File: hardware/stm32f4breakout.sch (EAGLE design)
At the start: 18 parts, among them U101 STM32F427VGT6, X101 24MHz

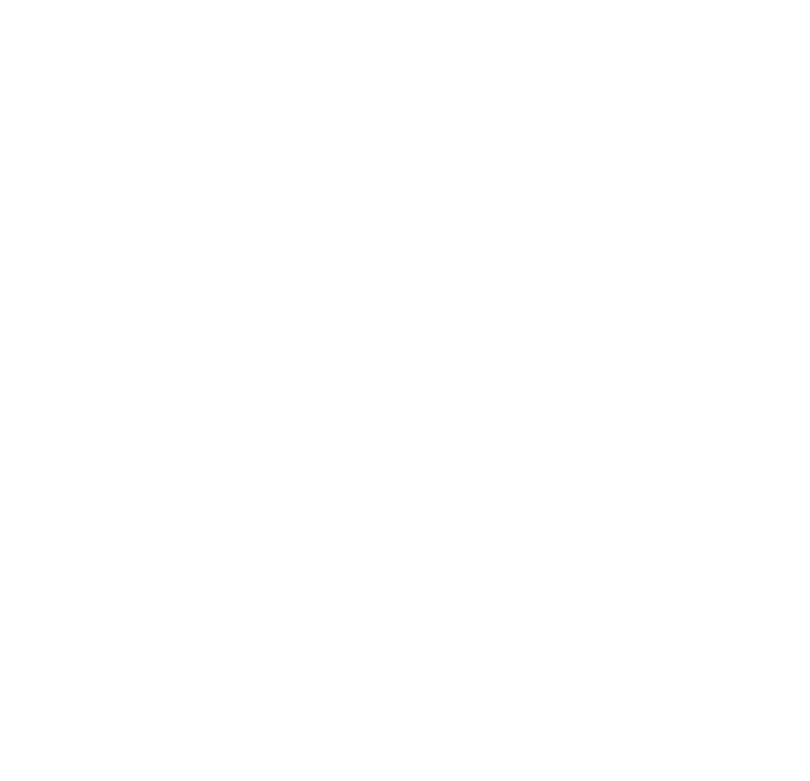
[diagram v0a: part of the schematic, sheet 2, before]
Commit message: Add 4.7uF decoupling cap
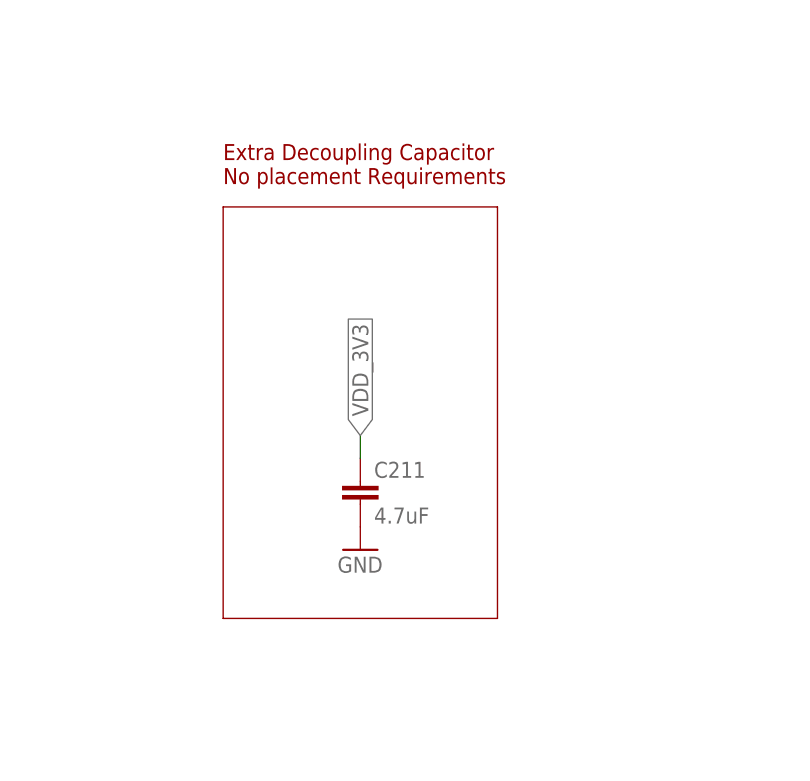
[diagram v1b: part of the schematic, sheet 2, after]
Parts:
- added C211: 4.7uF, quad:C-EUC0603
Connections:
- net GND: now also C211.2
- net VDD_3V3: now also C211.1
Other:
- note added: "Extra Decoupling Capacitor No placement Requirements"
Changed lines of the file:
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@@
 <grid distance="0.1" unitdist="inch" unit="inch" style="lines" multiple="1" display="no" altdistance="0.01" altunitdist="inch" altunit="inch"/>
 <layers>
-<layer number="1" name="Top" color="4" fill="1" visible="no" active="no"/>
-<layer number="2" name="Route2" color="1" fill="3" visible="no" active="no"/>
-<layer number="3" name="Route3" color="4" fill="3" visible="no" active="no"/>
-<layer number="4" name="Route4" color="1" fill="4" visible="no" active="no"/>
-<layer number="5" name="Route5" color="4" fill="4" visible="no" active="no"/>
-<layer number="6" name="Route6" color="1" fill="8" visible="no" active="no"/>
-<layer number="7" name="Route7" color="4" fill="8" visible="no" active="no"/>
-<layer number="8" name="Route8" color="1" fill="2" visible="no" active="no"/>
-<layer number="9" name="Route9" color="4" fill="2" visible="no" active="no"/>
-<layer number="10" name="Route10" color="1" fill="7" visible="no" active="no"/>
-<layer number="11" name="Route11" color="4" fill="7" visible="no" active="no"/>
-<layer number="12" name="Route12" color="1" fill="5" visible="no" active="no"/>
-<layer number="13" name="Route13" color="4" fill="5" visible="no" active="no"/>
-<layer number="14" name="Route14" color="1" fill="6" visible="no" active="no"/>
-<layer number="15" name="Route15" color="4" fill="6" visible="no" active="no"/>
-<layer number="16" name="Bottom" color="1" fill="1" visible="no" active="no"/>
-<layer number="17" name="Pads" color="2" fill="1" visible="no" active="no"/>
-<layer number="18" name="Vias" color="2" fill="1" visible="no" active="no"/>
-<layer number="19" name="Unrouted" color="6" fill="1" visible="no" active="no"/>
-<layer number="20" name="Dimension" color="24" fill="1" visible="no" active="no"/>
-<layer number="21" name="tPlace" color="7" fill="1" visible="no" active="no"/>
-<layer number="22" name="bPlace" color="7" fill="1" visible="no" active="no"/>
-<layer number="23" name="tOrigins" color="15" fill="1" visible="no" active="no"/>
-<layer number="24" name="bOrigins" color="15" fill="1" visible="no" active="no"/>
-<layer number="25" name="tNames" color="7" fill="1" visible="no" active="no"/>
-<layer number="26" name="bNames" color="7" fill="1" visible="no" active="no"/>
-<layer number="27" name="tValues" color="7" fill="1" visible="no" active="no"/>
-<layer number="28" name="bValues" color="7" fill="1" visible="no" active="no"/>
+<layer number="1" name="Top" color="4" fill="1" visible="yes" active="no"/>
+<layer number="2" name="Route2" color="1" fill="3" visible="yes" active="no"/>
+<layer number="3" name="Route3" color="4" fill="3" visible="yes" active="no"/>
+<layer number="4" name="Route4" color="1" fill="4" visible="yes" active="no"/>
+<layer number="5" name="Route5" color="4" fill="4" visible="yes" active="no"/>
+<layer number="6" name="Route6" color="1" fill="8" visible="yes" active="no"/>
+<layer number="7" name="Route7" color="4" fill="8" visible="yes" active="no"/>
+<layer number="8" name="Route8" color="1" fill="2" visible="yes" active="no"/>
+<layer number="9" name="Route9" color="4" fill="2" visible="yes" active="no"/>
+<layer number="10" name="Route10" color="1" fill="7" visible="yes" active="no"/>
+<layer number="11" name="Route11" color="4" fill="7" visible="yes" active="no"/>
+<layer number="12" name="Route12" color="1" fill="5" visible="yes" active="no"/>
+<layer number="13" name="Route13" color="4" fill="5" visible="yes" active="no"/>
+<layer number="14" name="Route14" color="1" fill="6" visible="yes" active="no"/>
+<layer number="15" name="Route15" color="4" fill="6" visible="yes" active="no"/>
+<layer number="16" name="Bottom" color="1" fill="1" visible="yes" active="no"/>
+<layer number="17" name="Pads" color="2" fill="1" visible="yes" active="no"/>
+<layer number="18" name="Vias" color="2" fill="1" visible="yes" active="no"/>
+<layer number="19" name="Unrouted" color="6" fill="1" visible="yes" active="no"/>
+<layer number="20" name="Dimension" color="24" fill="1" visible="yes" active="no"/>
+<layer number="21" name="tPlace" color="7" fill="1" visible="yes" active="no"/>
+<layer number="22" name="bPlace" color="7" fill="1" visible="yes" active="no"/>
+<layer number="23" name="tOrigins" color="15" fill="1" visible="yes" active="no"/>
+<layer number="24" name="bOrigins" color="15" fill="1" visible="yes" active="no"/>
+<layer number="25" name="tNames" color="7" fill="1" visible="yes" active="no"/>
+<layer number="26" name="bNames" color="7" fill="1" visible="yes" active="no"/>
+<layer number="27" name="tValues" color="7" fill="1" visible="yes" active="no"/>
+<layer number="28" name="bValues" color="7" fill="1" visible="yes" active="no"/>
 <layer number="29" name="tStop" color="7" fill="3" visible="no" active="no"/>
 <layer number="30" name="bStop" color="7" fill="6" visible="no" active="no"/>
@@
 <layer number="35" name="tGlue" color="7" fill="4" visible="no" active="no"/>
 <layer number="36" name="bGlue" color="7" fill="5" visible="no" active="no"/>
-<layer number="37" name="tTest" color="7" fill="1" visible="no" active="no"/>
-<layer number="38" name="bTest" color="7" fill="1" visible="no" active="no"/>
+<layer number="37" name="tTest" color="7" fill="1" visible="yes" active="no"/>
+<layer number="38" name="bTest" color="7" fill="1" visible="yes" active="no"/>
 <layer number="39" name="tKeepout" color="4" fill="11" visible="no" active="no"/>
 <layer number="40" name="bKeepout" color="1" fill="11" visible="no" active="no"/>
@@
 <layer number="44" name="Drills" color="7" fill="1" visible="no" active="no"/>
 <layer number="45" name="Holes" color="7" fill="1" visible="no" active="no"/>
-<layer number="46" name="Milling" color="3" fill="1" visible="no" active="no"/>
-<layer number="47" name="Measures" color="7" fill="1" visible="no" active="no"/>
-<layer number="48" name="Document" color="7" fill="1" visible="no" active="no"/>
-<layer number="49" name="Reference" color="7" fill="1" visible="no" active="no"/>
-<layer number="50" name="dxf" color="7" fill="1" visible="no" active="no"/>
-<layer number="51" name="tDocu" color="7" fill="1" visible="no" active="no"/>
-<layer number="52" name="bDocu" color="7" fill="1" visible="no" active="no"/>
-<layer number="53" name="tGND_GNDA" color="7" fill="9" visible="no" active="no"/>
-<layer number="54" name="bGND_GNDA" color="1" fill="9" visible="no" active="no"/>
-<layer number="56" name="wert" color="7" fill="1" visible="no" active="no"/>
-<layer number="57" name="tCAD" color="7" fill="1" visible="no" active="no"/>
-<layer number="59" name="tCarbon" color="7" fill="1" visible="no" active="no"/>
-<layer number="60" name="bCarbon" color="7" fill="1" visible="no" active="no"/>
+<layer number="46" name="Milling" color="3" fill="1" visible="yes" active="no"/>
+<layer number="47" name="Measures" color="7" fill="1" visible="yes" active="no"/>
+<layer number="48" name="Document" color="7" fill="1" visible="yes" active="no"/>
+<layer number="49" name="Reference" color="7" fill="1" visible="yes" active="no"/>
+<layer number="50" name="dxf" color="7" fill="1" visible="yes" active="no"/>
+<layer number="51" name="tDocu" color="7" fill="1" visible="yes" active="no"/>
+<layer number="52" name="bDocu" color="7" fill="1" visible="yes" active="no"/>
+<layer number="53" name="tGND_GNDA" color="7" fill="9" visible="yes" active="no"/>
+<layer number="54" name="bGND_GNDA" color="1" fill="9" visible="yes" active="no"/>
+<layer number="56" name="wert" color="7" fill="1" visible="yes" active="no"/>
+<layer number="57" name="tCAD" color="7" fill="1" visible="yes" active="no"/>
+<layer number="59" name="tCarbon" color="7" fill="1" visible="yes" active="no"/>
+<layer number="60" name="bCarbon" color="7" fill="1" visible="yes" active="no"/>
 <layer number="90" name="Modules" color="5" fill="1" visible="yes" active="yes"/>
 <layer number="91" name="Nets" color="2" fill="1" visible="yes" active="yes"/>
@@
 <part name="C210" library="quad" deviceset="C-EU" device="C0603" value="100nF"/>
 <part name="GND5" library="quad" deviceset="GND" device=""/>
+<part name="C211" library="quad" deviceset="C-EU" device="C0603" value="4.7uF"/>
+<part name="GND14" library="quad" deviceset="GND" device=""/>
 </parts>
 <sheets>
@@
 <text x="165.1" y="111.76" size="1.778" layer="94">Decoupling Capacitors
 Place as close to VDD pins as possible</text>
+<wire x1="162.56" y1="180.34" x2="193.04" y2="180.34" width="0.1524" layer="94"/>
+<wire x1="193.04" y1="180.34" x2="193.04" y2="134.62" width="0.1524" layer="94"/>
+<wire x1="193.04" y1="134.62" x2="162.56" y2="134.62" width="0.1524" layer="94"/>
+<wire x1="162.56" y1="134.62" x2="162.56" y2="180.34" width="0.1524" layer="94"/>
+<text x="162.56" y="182.88" size="1.778" layer="94">Extra Decoupling Capacitor
+No placement Requirements</text>
 </plain>
 <instances>
@@
 <instance part="C210" gate="G$1" x="223.52" y="81.28"/>
 <instance part="GND5" gate="1" x="223.52" y="73.66"/>
+<instance part="C211" gate="G$1" x="177.8" y="149.86"/>
+<instance part="GND14" gate="1" x="177.8" y="142.24"/>
 </instances>
 <busses>
@@
 <pinref part="GND5" gate="1" pin="GND"/>
 </segment>
+<segment>
+<pinref part="C211" gate="G$1" pin="2"/>
+<pinref part="GND14" gate="1" pin="GND"/>
+</segment>
 </net>
 <net name="NRST" class="0">
@@
 <wire x1="81.28" y1="124.46" x2="71.12" y2="124.46" width="0.1524" layer="91"/>
 </segment>
-</net>
+<segment>
+<pinref part="C211" gate="G$1" pin="1"/>
+<wire x1="177.8" y1="152.4" x2="177.8" y2="154.94" width="0.1524" layer="91"/>
+<label x="177.8" y="154.94" size="1.778" layer="95" rot="R90" xref="yes"/>
+</segment>
+</net>
